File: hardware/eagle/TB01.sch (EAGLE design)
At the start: 26 parts, among them J1 CON_TERMINAL_BLOCK_02-5MM, J4 CON_TERMINAL_BLOCK_02-5MM, J5 CON_TERMINAL_BLOCK_03-5MM, T1 BT138-V, T2 BT138-V

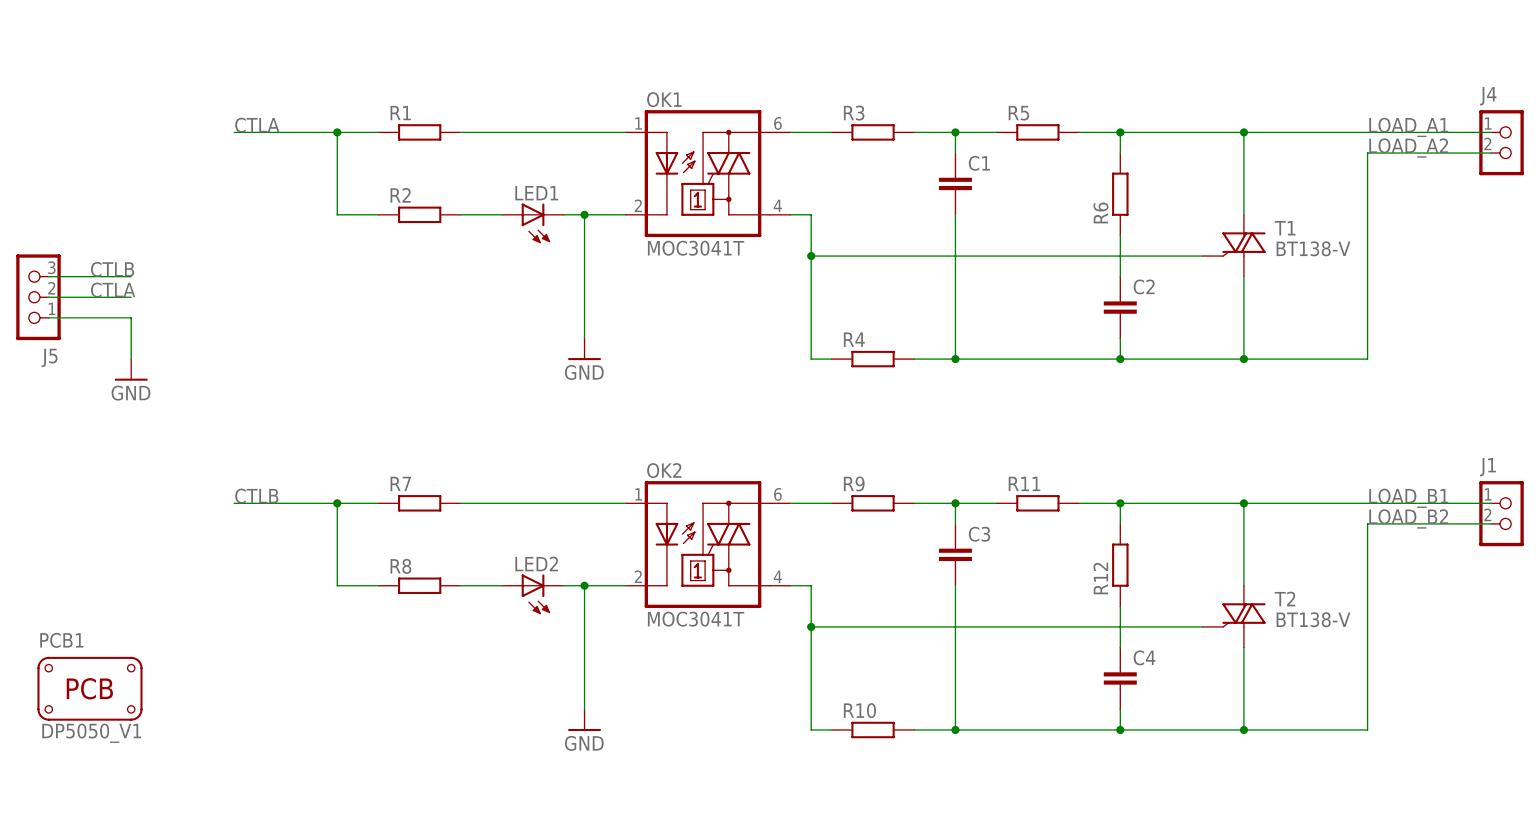
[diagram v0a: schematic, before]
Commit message: layout altered, resistor values
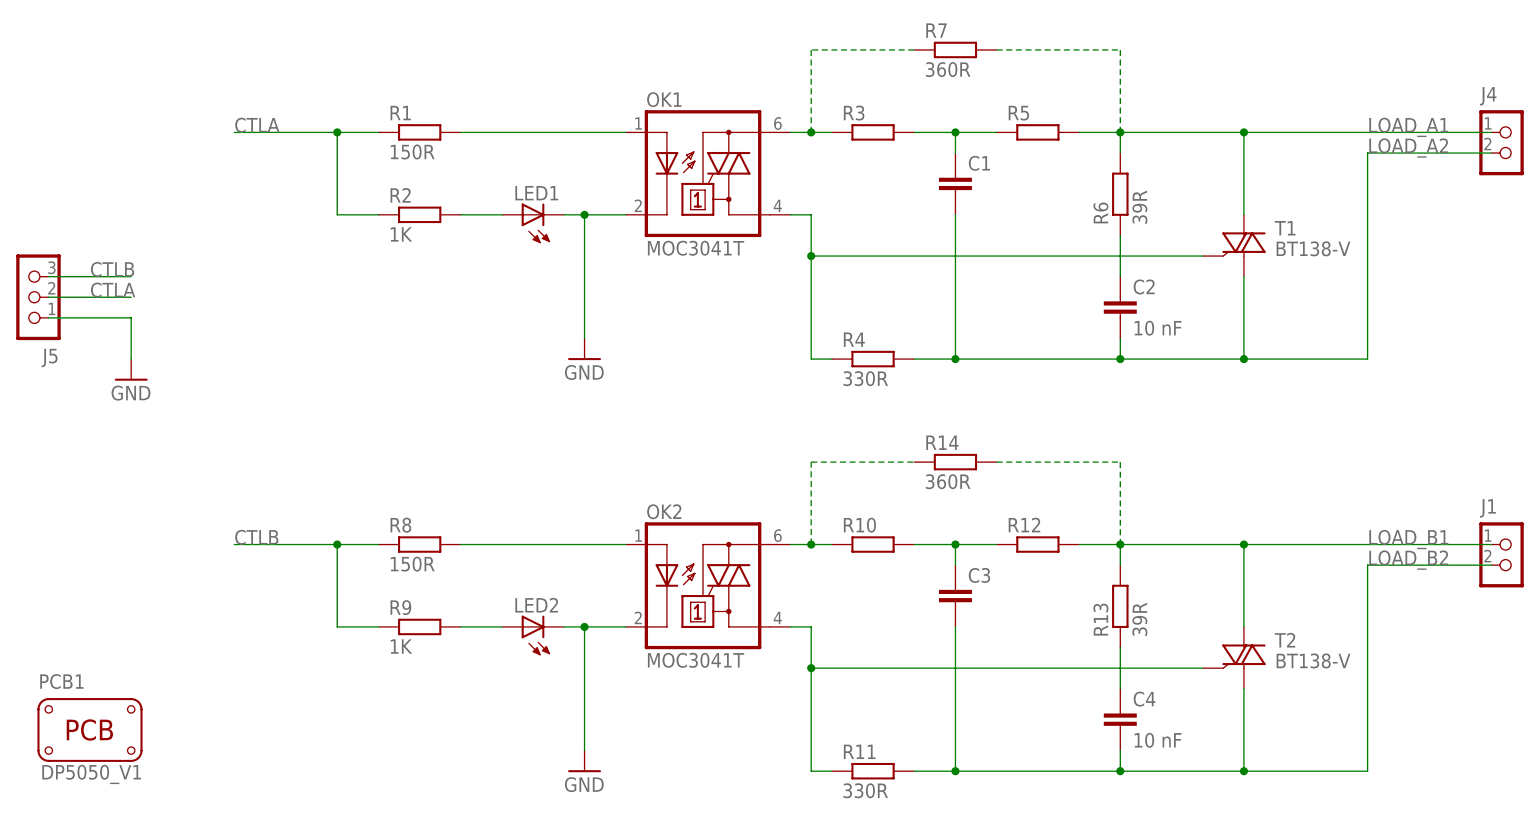
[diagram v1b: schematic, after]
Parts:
- added R13: 39R, rcl:R-EU_0207/7
- added R14: 360R, rcl:R-EU_0207/7
- C2, C4: value (none) -> 10 nF
- R1, R8: value (none) -> 150R
- R11, R4: value (none) -> 330R
- R2, R9: value (none) -> 1K
- R6: value (none) -> 39R
- R7: value (none) -> 360R
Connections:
- net CTLB: now also R9.1; no longer R7.1
- net LOAD_A1: now also R7.2
- net LOAD_B1: now also R13.2, R14.2; no longer R11.2
- net LOAD_B2: now also R11.2; no longer R10.2
- net N$10: now also R10.2, R12.1; no longer R11.1, R9.2
- net N$11: now also R13.1; no longer R12.1
- net N$12: now also R11.1; no longer R10.1
- net N$3: now also R7.1
- net N$6: now also R9.2; no longer R8.2
- net N$8: now also R8.2; no longer R7.2
- net N$9: now also R10.1, R14.1; no longer R9.1
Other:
- moved on the sheet: C3, C4, J1, LED2, OK2, PCB1, R10, R11, R12, R7, R8, R9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

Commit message: redesign without snubbers
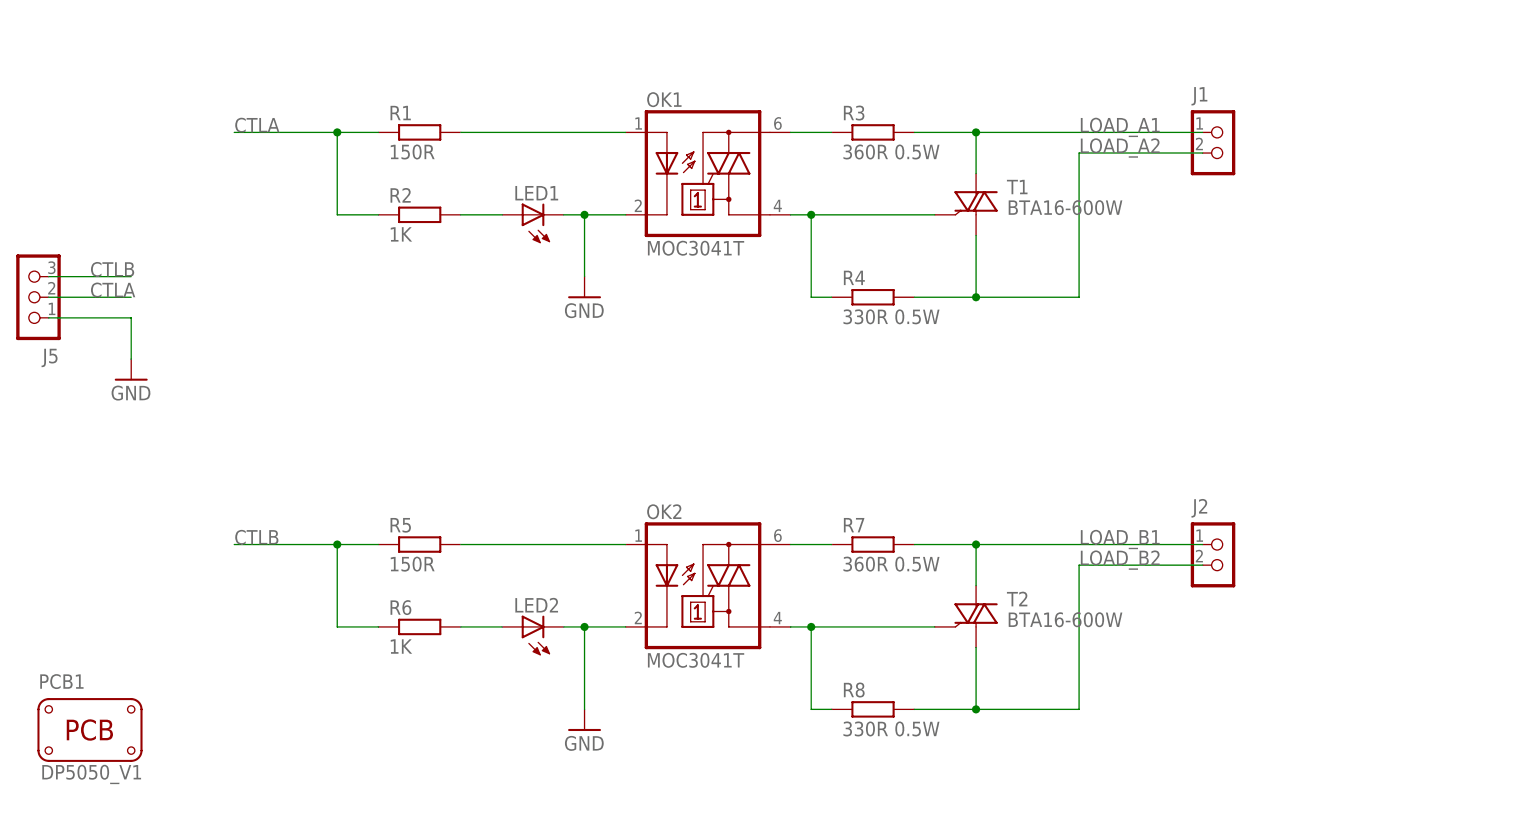
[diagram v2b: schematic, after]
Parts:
- removed C1, C3: (no value), rcl:C-EU025-025X050
- removed C2, C4: 10 nF, rcl:C-EU025-025X050
- removed J4: CON_TERMINAL_BLOCK_02-5MM, dp_devices:CON_TERMINAL_BLOCK_02-5MM
- removed R10, R12: (no value), rcl:R-EU_0207/7
- removed R11: 330R, rcl:R-EU_0207/7
- removed R13: 39R, rcl:R-EU_0207/7
- removed R14: 360R, rcl:R-EU_0207/7
- removed R9: 1K, rcl:R-EU_0207/7
- added J2: CON_TERMINAL_BLOCK_02-5MM, dp_devices:CON_TERMINAL_BLOCK_02-5MM
- R3: value (none) -> 360R 0.5W; device rcl:R-EU_0207/7 -> rcl:R-EU_0411/3V
- R4: value 330R -> 330R 0.5W; device rcl:R-EU_0207/7 -> rcl:R-EU_0411/3V
- R5: value (none) -> 150R
- R6: value 39R -> 1K
- R7: value 360R -> 360R 0.5W; device rcl:R-EU_0207/7 -> rcl:R-EU_0411/3V
- R8: value 150R -> 330R 0.5W; device rcl:R-EU_0207/7 -> rcl:R-EU_0411/3V
- T1, T2: value BT138-V -> BTA16-600W
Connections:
- removed net N$10: C3.1, R10.2, R12.1
- removed net N$11: C4.1, R13.1
- removed net N$12: OK2.A1, R11.1, T2.G
- removed net N$9: OK2.A2, R10.1, R14.1
- net CTLB: now also R5.1, R6.1; no longer R8.1, R9.1
- net LOAD_A1: now also J1.1, R3.2; no longer J4.1, R5.2, R6.2, R7.2
- net LOAD_A2: now also J1.2; no longer C1.2, C2.2, J4.2
- net LOAD_B1: now also J2.1, R7.2; no longer J1.1, R12.2, R13.2, R14.2
- net LOAD_B2: now also J2.2, R8.2; no longer C3.2, C4.2, J1.2, R11.2
- net N$3: no longer R7.1
- net N$4: now also OK2.A2, R7.1; no longer C1.1, R3.2, R5.1
- net N$6: now also R6.2; no longer R9.2
- net N$7: now also OK2.A1, R8.1, T2.G; no longer C2.1, R6.1
- net N$8: now also R5.2; no longer R8.2
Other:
- moved on the sheet: J1, R4, R5, R6, R7, R8, T1, T2

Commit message: splay pin triac package
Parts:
- T1, T2: device triac:BT138-V -> triac:BT138
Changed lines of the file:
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@@
 <grid distance="0.1" unitdist="inch" unit="inch" style="lines" multiple="1" display="no" altdistance="0.01" altunitdist="inch" altunit="inch"/>
 <layers>
-<layer number="1" name="Top" color="4" fill="1" visible="no" active="no"/>
-<layer number="2" name="Route2" color="1" fill="3" visible="no" active="no"/>
-<layer number="3" name="Route3" color="4" fill="3" visible="no" active="no"/>
-<layer number="4" name="Route4" color="1" fill="4" visible="no" active="no"/>
-<layer number="5" name="Route5" color="4" fill="4" visible="no" active="no"/>
-<layer number="6" name="Route6" color="1" fill="8" visible="no" active="no"/>
-<layer number="7" name="Route7" color="4" fill="8" visible="no" active="no"/>
-<layer number="8" name="Route8" color="1" fill="2" visible="no" active="no"/>
-<layer number="9" name="Route9" color="4" fill="2" visible="no" active="no"/>
-<layer number="10" name="Route10" color="1" fill="7" visible="no" active="no"/>
-<layer number="11" name="Route11" color="4" fill="7" visible="no" active="no"/>
-<layer number="12" name="Route12" color="1" fill="5" visible="no" active="no"/>
-<layer number="13" name="Route13" color="4" fill="5" visible="no" active="no"/>
-<layer number="14" name="Route14" color="1" fill="6" visible="no" active="no"/>
-<layer number="15" name="Route15" color="4" fill="6" visible="no" active="no"/>
-<layer number="16" name="Bottom" color="1" fill="1" visible="no" active="no"/>
-<layer number="17" name="Pads" color="2" fill="1" visible="no" active="no"/>
-<layer number="18" name="Vias" color="2" fill="1" visible="no" active="no"/>
-<layer number="19" name="Unrouted" color="6" fill="1" visible="no" active="no"/>
-<layer number="20" name="Dimension" color="15" fill="1" visible="no" active="no"/>
-<layer number="21" name="tPlace" color="16" fill="1" visible="no" active="no"/>
-<layer number="22" name="bPlace" color="14" fill="1" visible="no" active="no"/>
-<layer number="23" name="tOrigins" color="15" fill="1" visible="no" active="no"/>
-<layer number="24" name="bOrigins" color="15" fill="1" visible="no" active="no"/>
-<layer number="25" name="tNames" color="7" fill="1" visible="no" active="no"/>
-<layer number="26" name="bNames" color="7" fill="1" visible="no" active="no"/>
-<layer number="27" name="tValues" color="7" fill="1" visible="no" active="no"/>
-<layer number="28" name="bValues" color="7" fill="1" visible="no" active="no"/>
+<layer number="1" name="Top" color="4" fill="1" visible="yes" active="no"/>
+<layer number="2" name="Route2" color="1" fill="3" visible="yes" active="no"/>
+<layer number="3" name="Route3" color="4" fill="3" visible="yes" active="no"/>
+<layer number="4" name="Route4" color="1" fill="4" visible="yes" active="no"/>
+<layer number="5" name="Route5" color="4" fill="4" visible="yes" active="no"/>
+<layer number="6" name="Route6" color="1" fill="8" visible="yes" active="no"/>
+<layer number="7" name="Route7" color="4" fill="8" visible="yes" active="no"/>
+<layer number="8" name="Route8" color="1" fill="2" visible="yes" active="no"/>
+<layer number="9" name="Route9" color="4" fill="2" visible="yes" active="no"/>
+<layer number="10" name="Route10" color="1" fill="7" visible="yes" active="no"/>
+<layer number="11" name="Route11" color="4" fill="7" visible="yes" active="no"/>
+<layer number="12" name="Route12" color="1" fill="5" visible="yes" active="no"/>
+<layer number="13" name="Route13" color="4" fill="5" visible="yes" active="no"/>
+<layer number="14" name="Route14" color="1" fill="6" visible="yes" active="no"/>
+<layer number="15" name="Route15" color="4" fill="6" visible="yes" active="no"/>
+<layer number="16" name="Bottom" color="1" fill="1" visible="yes" active="no"/>
+<layer number="17" name="Pads" color="2" fill="1" visible="yes" active="no"/>
+<layer number="18" name="Vias" color="2" fill="1" visible="yes" active="no"/>
+<layer number="19" name="Unrouted" color="6" fill="1" visible="yes" active="no"/>
+<layer number="20" name="Dimension" color="15" fill="1" visible="yes" active="no"/>
+<layer number="21" name="tPlace" color="14" fill="1" visible="yes" active="no"/>
+<layer number="22" name="bPlace" color="13" fill="1" visible="yes" active="no"/>
+<layer number="23" name="tOrigins" color="15" fill="1" visible="yes" active="no"/>
+<layer number="24" name="bOrigins" color="15" fill="1" visible="yes" active="no"/>
+<layer number="25" name="tNames" color="7" fill="1" visible="yes" active="no"/>
+<layer number="26" name="bNames" color="7" fill="1" visible="yes" active="no"/>
+<layer number="27" name="tValues" color="7" fill="1" visible="yes" active="no"/>
+<layer number="28" name="bValues" color="7" fill="1" visible="yes" active="no"/>
 <layer number="29" name="tStop" color="7" fill="3" visible="no" active="no"/>
 <layer number="30" name="bStop" color="7" fill="6" visible="no" active="no"/>
@@
 <layer number="35" name="tGlue" color="7" fill="4" visible="no" active="no"/>
 <layer number="36" name="bGlue" color="7" fill="5" visible="no" active="no"/>
-<layer number="37" name="tTest" color="7" fill="1" visible="no" active="no"/>
-<layer number="38" name="bTest" color="7" fill="1" visible="no" active="no"/>
+<layer number="37" name="tTest" color="7" fill="1" visible="yes" active="no"/>
+<layer number="38" name="bTest" color="7" fill="1" visible="yes" active="no"/>
 <layer number="39" name="tKeepout" color="4" fill="11" visible="no" active="no"/>
 <layer number="40" name="bKeepout" color="1" fill="11" visible="no" active="no"/>
@@
 <layer number="44" name="Drills" color="7" fill="1" visible="no" active="no"/>
 <layer number="45" name="Holes" color="7" fill="1" visible="no" active="no"/>
-<layer number="46" name="Milling" color="3" fill="1" visible="no" active="no"/>
-<layer number="47" name="Measures" color="7" fill="1" visible="no" active="no"/>
-<layer number="48" name="Document" color="7" fill="1" visible="no" active="no"/>
-<layer number="49" name="Reference" color="7" fill="1" visible="no" active="no"/>
-<layer number="50" name="dxf" color="7" fill="1" visible="no" active="no"/>
-<layer number="51" name="tDocu" color="6" fill="1" visible="no" active="no"/>
-<layer number="52" name="bDocu" color="7" fill="1" visible="no" active="no"/>
-<layer number="53" name="tGND_GNDA" color="7" fill="9" visible="no" active="no"/>
-<layer number="54" name="bGND_GNDA" color="1" fill="9" visible="no" active="no"/>
-<layer number="56" name="wert" color="7" fill="1" visible="no" active="no"/>
+<layer number="46" name="Milling" color="3" fill="1" visible="yes" active="no"/>
+<layer number="47" name="Measures" color="7" fill="1" visible="yes" active="no"/>
+<layer number="48" name="Document" color="7" fill="1" visible="yes" active="no"/>
+<layer number="49" name="Reference" color="7" fill="1" visible="yes" active="no"/>
+<layer number="50" name="dxf" color="7" fill="1" visible="yes" active="no"/>
+<layer number="51" name="tDocu" color="6" fill="1" visible="yes" active="no"/>
+<layer number="52" name="bDocu" color="7" fill="1" visible="yes" active="no"/>
+<layer number="53" name="tGND_GNDA" color="7" fill="9" visible="yes" active="no"/>
+<layer number="54" name="bGND_GNDA" color="1" fill="9" visible="yes" active="no"/>
+<layer number="56" name="wert" color="7" fill="1" visible="yes" active="no"/>
 <layer number="91" name="Nets" color="2" fill="1" visible="yes" active="yes"/>
 <layer number="92" name="Busses" color="1" fill="1" visible="yes" active="yes"/>
@@
 <part name="LED1" library="SparkFun" deviceset="LED" device="3MM"/>
 <part name="R4" library="rcl" deviceset="R-EU_" device="0411/3V" value="330R 0.5W"/>
-<part name="T1" library="triac" deviceset="BT138" device="-V" value="BTA16-600W"/>
+<part name="T1" library="triac" deviceset="BT138" device="" value="BTA16-600W"/>
 <part name="GND1" library="SparkFun" deviceset="GND" device=""/>
 <part name="J2" library="dp_devices" deviceset="CON_TERMINAL_BLOCK_02" device="-5MM"/>
@@
 <part name="R6" library="rcl" deviceset="R-EU_" device="0207/7" value="1K"/>
 <part name="LED2" library="SparkFun" deviceset="LED" device="3MM"/>
-<part name="T2" library="triac" deviceset="BT138" device="-V" value="BTA16-600W"/>
+<part name="T2" library="triac" deviceset="BT138" device="" value="BTA16-600W"/>
 <part name="R3" library="rcl" deviceset="R-EU_" device="0411/3V" value="360R 0.5W"/>
 <part name="R7" library="rcl" deviceset="R-EU_" device="0411/3V" value="360R 0.5W"/>
